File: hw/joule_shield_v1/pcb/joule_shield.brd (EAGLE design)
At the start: 160 x 100 mm, 55 parts, among them U1 BQ25892PWQFN-24, U2 FAN8623WLCSP16, U3 TPS63201PVSON-14, U4 TLV62084PWSON-8

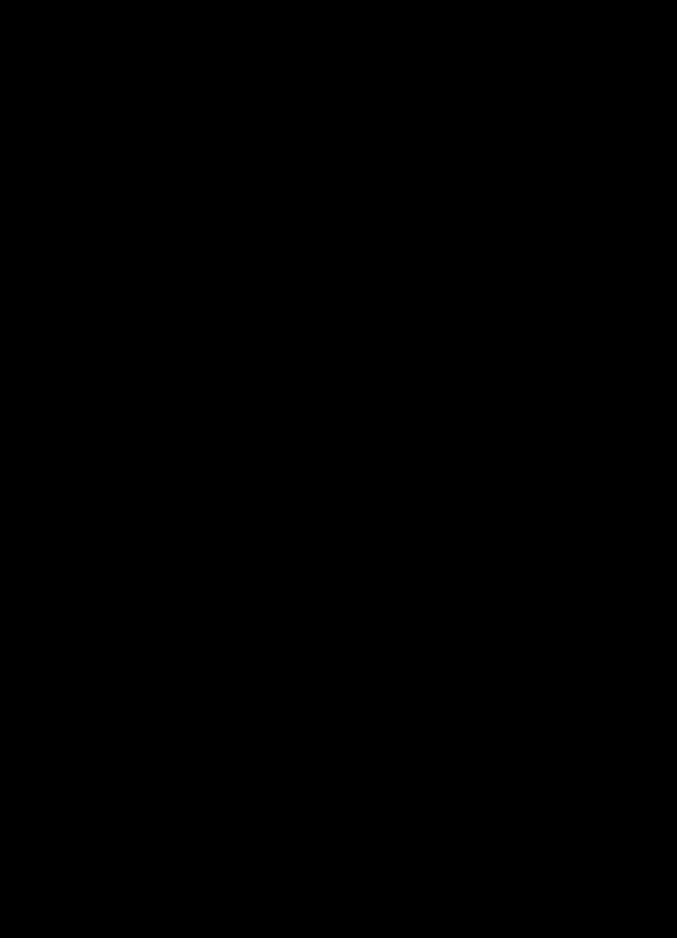
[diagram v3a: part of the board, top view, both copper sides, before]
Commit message: Schematic for USB power switch.
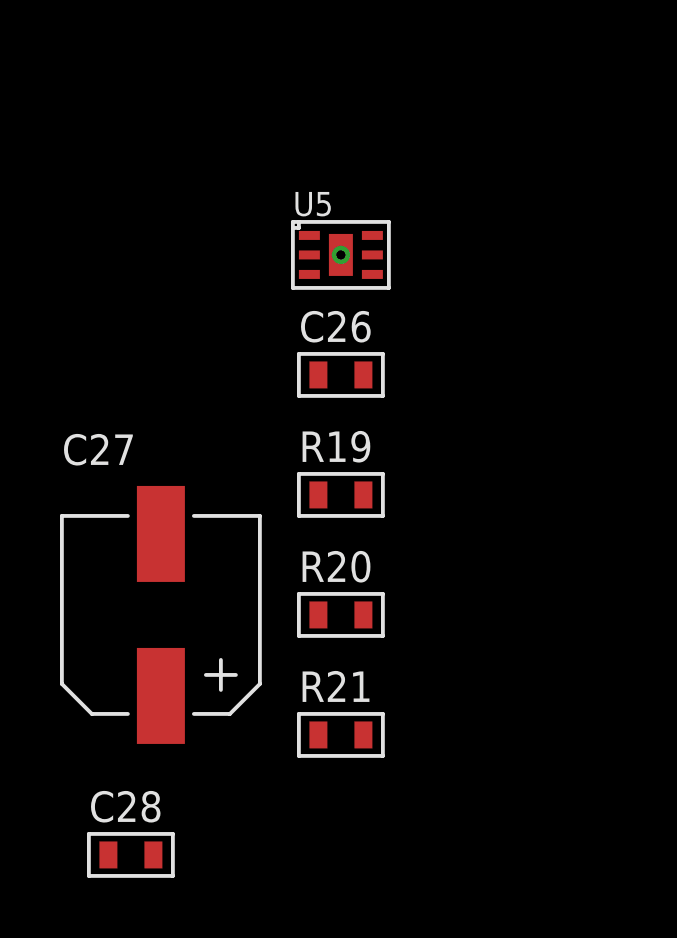
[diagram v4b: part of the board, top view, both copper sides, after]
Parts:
- added C26: 10uF, mf_passives:C0603
- added C27: 100uF, mf_passives:CP6.3MM
- added C28: 0.1uF, mf_passives:C0603
- added R19, R20: 100k, mf_passives:R0603
- added R21: 15k, mf_passives:R0603
- added U5: TPS2553PWSON-6, joule_shield:PWSON-6
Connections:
- new net N$22: R19.P$2, U5.3
- new net N$24: R20.P$2, U5.4
- new net N$29: R21.P$1, U5.2
- new net V5P0V_USBA: C27.P$1, C28.P$1, U5.1
- net GND: now also C26.P$2, C27.P$2, C28.P$2, R21.P$2, U5.5, U5.G0, U5.G1
- net V5P0V: now also C26.P$1, R19.P$1, R20.P$1, U5.6
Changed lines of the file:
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@@
 <attribute name="WATTAGE" value="" x="-109" y="67" size="1.778" layer="27" display="off"/>
+</element>
+<element name="U5" library="joule_shield" package="PWSON-6" value="TPS2553PWSON-6" x="-109" y="-3"/>
+<element name="C26" library="mf_passives" package="C0603" value="10uF" x="-109" y="-7">
+<attribute name="HOUSEPART" value="" x="-109" y="-7" size="1.778" layer="27" display="off"/>
+<attribute name="TOLERANCE" value="" x="-109" y="-7" size="1.778" layer="27" display="off"/>
+<attribute name="MPN" value="C1608X5R1E106M080AC" x="-109" y="-7" size="1.778" layer="27" display="off"/>
+<attribute name="POPULATE" value="1" x="-109" y="-7" size="1.778" layer="27" display="off"/>
+<attribute name="DIELECTRIC" value="" x="-109" y="-7" size="1.778" layer="27" display="off"/>
+<attribute name="VOLTAGE" value="" x="-109" y="-7" size="1.778" layer="27" display="off"/>
+<attribute name="URL" value="" x="-109" y="-7" size="1.778" layer="27" display="off"/>
+<attribute name="DPN" value="445-9015-1-ND" x="-109" y="-7" size="1.778" layer="27" display="off"/>
+</element>
+<element name="R19" library="mf_passives" package="R0603" value="100k" x="-109" y="-11">
+<attribute name="HOUSEPART" value="" x="-109" y="-11" size="1.778" layer="27" display="off"/>
+<attribute name="TOLERANCE" value="" x="-109" y="-11" size="1.778" layer="27" display="off"/>
+<attribute name="MPN" value="MF-RES-0603-100K" x="-109" y="-11" size="1.778" layer="27" display="off"/>
+<attribute name="POPULATE" value="1" x="-109" y="-11" size="1.778" layer="27" display="off"/>
+<attribute name="VOLTAGE" value="" x="-109" y="-11" size="1.778" layer="27" display="off"/>
+<attribute name="URL" value="" x="-109" y="-11" size="1.778" layer="27" display="off"/>
+<attribute name="WATTAGE" value="" x="-109" y="-11" size="1.778" layer="27" display="off"/>
+</element>
+<element name="R20" library="mf_passives" package="R0603" value="100k" x="-109" y="-15">
+<attribute name="HOUSEPART" value="" x="-109" y="-15" size="1.778" layer="27" display="off"/>
+<attribute name="TOLERANCE" value="" x="-109" y="-15" size="1.778" layer="27" display="off"/>
+<attribute name="MPN" value="MF-RES-0603-100K" x="-109" y="-15" size="1.778" layer="27" display="off"/>
+<attribute name="POPULATE" value="1" x="-109" y="-15" size="1.778" layer="27" display="off"/>
+<attribute name="VOLTAGE" value="" x="-109" y="-15" size="1.778" layer="27" display="off"/>
+<attribute name="URL" value="" x="-109" y="-15" size="1.778" layer="27" display="off"/>
+<attribute name="WATTAGE" value="" x="-109" y="-15" size="1.778" layer="27" display="off"/>
+</element>
+<element name="R21" library="mf_passives" package="R0603" value="15k" x="-109" y="-19">
+<attribute name="HOUSEPART" value="" x="-109" y="-19" size="1.778" layer="27" display="off"/>
+<attribute name="TOLERANCE" value="" x="-109" y="-19" size="1.778" layer="27" display="off"/>
+<attribute name="MPN" value="MF-RES-0603-15K" x="-109" y="-19" size="1.778" layer="27" display="off"/>
+<attribute name="POPULATE" value="1" x="-109" y="-19" size="1.778" layer="27" display="off"/>
+<attribute name="VOLTAGE" value="" x="-109" y="-19" size="1.778" layer="27" display="off"/>
+<attribute name="URL" value="" x="-109" y="-19" size="1.778" layer="27" display="off"/>
+<attribute name="WATTAGE" value="" x="-109" y="-19" size="1.778" layer="27" display="off"/>
+</element>
+<element name="C27" library="mf_passives" package="CP6.3MM" value="100uF" x="-115" y="-15">
+<attribute name="HOUSEPART" value="" x="-115" y="-15" size="1.778" layer="27" display="off"/>
+<attribute name="TOLERANCE" value="" x="-115" y="-15" size="1.778" layer="27" display="off"/>
+<attribute name="MPN" value="MF-CAP-6.3MM-100uF" x="-115" y="-15" size="1.778" layer="27" display="off"/>
+<attribute name="POPULATE" value="1" x="-115" y="-15" size="1.778" layer="27" display="off"/>
+<attribute name="VOTLAGE" value="" x="-115" y="-15" size="1.778" layer="27" display="off"/>
+<attribute name="URL" value="" x="-115" y="-15" size="1.778" layer="27" display="off"/>
+</element>
+<element name="C28" library="mf_passives" package="C0603" value="0.1uF" x="-116" y="-23">
+<attribute name="HOUSEPART" value="" x="-116" y="-23" size="1.778" layer="27" display="off"/>
+<attribute name="TOLERANCE" value="" x="-116" y="-23" size="1.778" layer="27" display="off"/>
+<attribute name="MPN" value="MF-CAP-0603-0.1uF" x="-116" y="-23" size="1.778" layer="27" display="off"/>
+<attribute name="POPULATE" value="1" x="-116" y="-23" size="1.778" layer="27" display="off"/>
+<attribute name="DIELECTRIC" value="" x="-116" y="-23" size="1.778" layer="27" display="off"/>
+<attribute name="VOLTAGE" value="" x="-116" y="-23" size="1.778" layer="27" display="off"/>
+<attribute name="URL" value="" x="-116" y="-23" size="1.778" layer="27" display="off"/>
 </element>
 </elements>
@@
 <contactref element="C25" pad="P$2"/>
 <contactref element="R17" pad="P$2"/>
-<wire x1="-108.25" y1="87" x2="-108.25" y2="71" width="0" layer="19" extent="1-1"/>
-<wire x1="-108.25" y1="91" x2="-108.25" y2="87" width="0" layer="19" extent="1-1"/>
-<wire x1="-108.25" y1="95" x2="-108.25" y2="91" width="0" layer="19" extent="1-1"/>
-<wire x1="-108.25" y1="105" x2="-108.25" y2="95" width="0" layer="19" extent="1-1"/>
-<wire x1="-108.25" y1="109" x2="-108.25" y2="105" width="0" layer="19" extent="1-1"/>
-<wire x1="-109" y1="113" x2="-108.25" y2="109" width="0" layer="19" extent="1-1"/>
-<wire x1="-109.95" y1="113.25" x2="-109" y2="113" width="0" layer="19" extent="1-1"/>
-<wire x1="-109.95" y1="112.75" x2="-109.95" y2="113.25" width="0" layer="19" extent="1-1"/>
-<wire x1="-77.25" y1="62" x2="-109.95" y2="113.25" width="0" layer="19" extent="1-1"/>
+<contactref element="C26" pad="P$2"/>
+<contactref element="U5" pad="G0"/>
+<contactref element="U5" pad="5"/>
+<contactref element="U5" pad="G1"/>
+<contactref element="R21" pad="P$2"/>
+<contactref element="C27" pad="P$2"/>
+<contactref element="C28" pad="P$2"/>
+<wire x1="-108.25" y1="-19" x2="-115.25" y2="-23" width="0" layer="19" extent="1-1"/>
+<wire x1="-115" y1="-12.3" x2="-108.25" y2="-19" width="0" layer="19" extent="1-1"/>
+<wire x1="-108.25" y1="-7" x2="-115" y2="-12.3" width="0" layer="19" extent="1-1"/>
+<wire x1="-107.95" y1="-3" x2="-108.25" y2="-7" width="0" layer="19" extent="1-1"/>
+<wire x1="-109" y1="-3" x2="-107.95" y2="-3" width="0" layer="19" extent="1-1"/>
+<wire x1="-77.25" y1="62" x2="-107.95" y2="-3" width="0" layer="19" extent="1-1"/>
 <wire x1="-77.25" y1="66" x2="-77.25" y2="62" width="0" layer="19" extent="1-1"/>
 <wire x1="-77.25" y1="70" x2="-77.25" y2="66" width="0" layer="19" extent="1-1"/>
@@
 <wire x1="-14.49" y1="82.55" x2="-18.3" y2="82.55" width="0" layer="19" extent="1-1"/>
 <wire x1="-22.11" y1="86.36" x2="-18.3" y2="82.55" width="0" layer="19" extent="1-1"/>
+<wire x1="-108.25" y1="109" x2="-79.4" y2="110" width="0" layer="19" extent="1-1"/>
+<wire x1="-108.25" y1="105" x2="-108.25" y2="109" width="0" layer="19" extent="1-1"/>
+<wire x1="-109" y1="113" x2="-108.25" y2="109" width="0" layer="19" extent="1-1"/>
+<wire x1="-109.95" y1="113.25" x2="-109" y2="113" width="0" layer="19" extent="1-1"/>
+<wire x1="-109.95" y1="112.75" x2="-109.95" y2="113.25" width="0" layer="19" extent="1-1"/>
+<wire x1="-108.25" y1="95" x2="-108.25" y2="105" width="0" layer="19" extent="1-1"/>
+<wire x1="-108.25" y1="91" x2="-108.25" y2="95" width="0" layer="19" extent="1-1"/>
+<wire x1="-108.25" y1="87" x2="-108.25" y2="91" width="0" layer="19" extent="1-1"/>
+<wire x1="-108.25" y1="71" x2="-108.25" y2="87" width="0" layer="19" extent="1-1"/>
 </signal>
 <signal name="N$2">
@@
 <contactref element="C12" pad="P$1"/>
 <contactref element="R12" pad="P$1"/>
+<contactref element="C26" pad="P$1"/>
+<contactref element="U5" pad="6"/>
+<contactref element="R19" pad="P$1"/>
+<contactref element="R20" pad="P$1"/>
+<wire x1="-109.75" y1="-11" x2="-109.75" y2="-15" width="0" layer="19" extent="1-1"/>
+<wire x1="-109.75" y1="-7" x2="-109.75" y2="-11" width="0" layer="19" extent="1-1"/>
+<wire x1="-107.95" y1="-2.35" x2="-109.75" y2="-7" width="0" layer="19" extent="1-1"/>
+<wire x1="-54.75" y1="67" x2="-107.95" y2="-2.35" width="0" layer="19" extent="1-1"/>
+<wire x1="-54.75" y1="71" x2="-54.75" y2="67" width="0" layer="19" extent="1-1"/>
+<wire x1="-54.75" y1="75" x2="-54.75" y2="71" width="0" layer="19" extent="1-1"/>
+<wire x1="-53.4" y1="107.2" x2="-54.75" y2="75" width="0" layer="19" extent="1-1"/>
 <wire x1="-53.8" y1="107.2" x2="-53.4" y2="107.2" width="0" layer="19" extent="1-1"/>
-<wire x1="-54.75" y1="75" x2="-53.4" y2="107.2" width="0" layer="19" extent="1-1"/>
-<wire x1="-54.75" y1="71" x2="-54.75" y2="75" width="0" layer="19" extent="1-1"/>
-<wire x1="-54.75" y1="67" x2="-54.75" y2="71" width="0" layer="19" extent="1-1"/>
 </signal>
 <signal name="VREGN">
@@
 <wire x1="-18.485" y1="71.1" x2="-19.8" y2="74.93" width="0" layer="19" extent="1-1"/>
 </signal>
+<signal name="N$22">
+<contactref element="R19" pad="P$2"/>
+<contactref element="U5" pad="3"/>
+<wire x1="-110.05" y1="-3.65" x2="-108.25" y2="-11" width="0" layer="19" extent="1-1"/>
+</signal>
+<signal name="N$24">
+<contactref element="R20" pad="P$2"/>
+<contactref element="U5" pad="4"/>
+<wire x1="-107.95" y1="-3.65" x2="-108.25" y2="-15" width="0" layer="19" extent="1-1"/>
+</signal>
+<signal name="N$29">
+<contactref element="U5" pad="2"/>
+<contactref element="R21" pad="P$1"/>
+<wire x1="-110.05" y1="-3" x2="-109.75" y2="-19" width="0" layer="19" extent="1-1"/>
+</signal>
+<signal name="V5P0V_USBA">
+<contactref element="U5" pad="1"/>
+<contactref element="C27" pad="P$1"/>
+<contactref element="C28" pad="P$1"/>
+<wire x1="-115" y1="-17.7" x2="-116.75" y2="-23" width="0" layer="19" extent="1-1"/>
+<wire x1="-110.05" y1="-2.35" x2="-115" y2="-17.7" width="0" layer="19" extent="1-1"/>
+</signal>
 </signals>

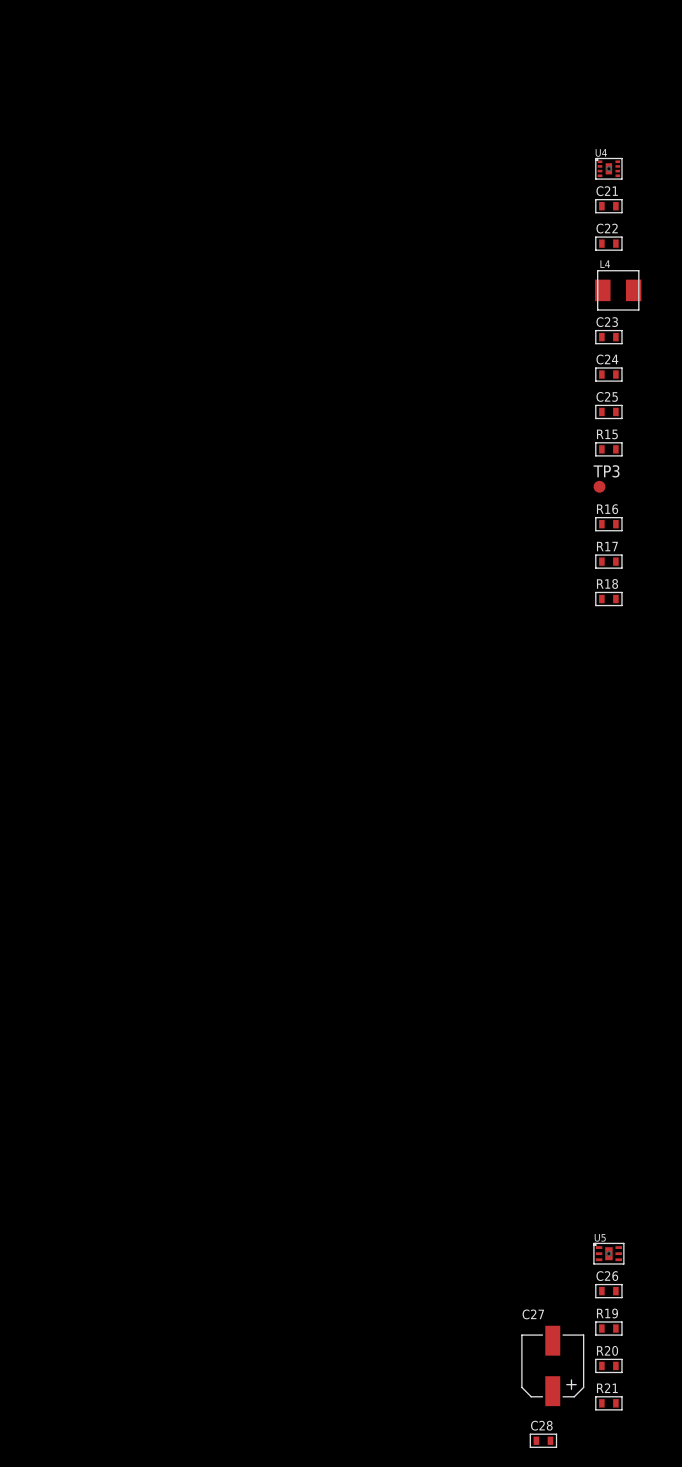
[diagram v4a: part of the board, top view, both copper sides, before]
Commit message: Schematic for serial level converters.
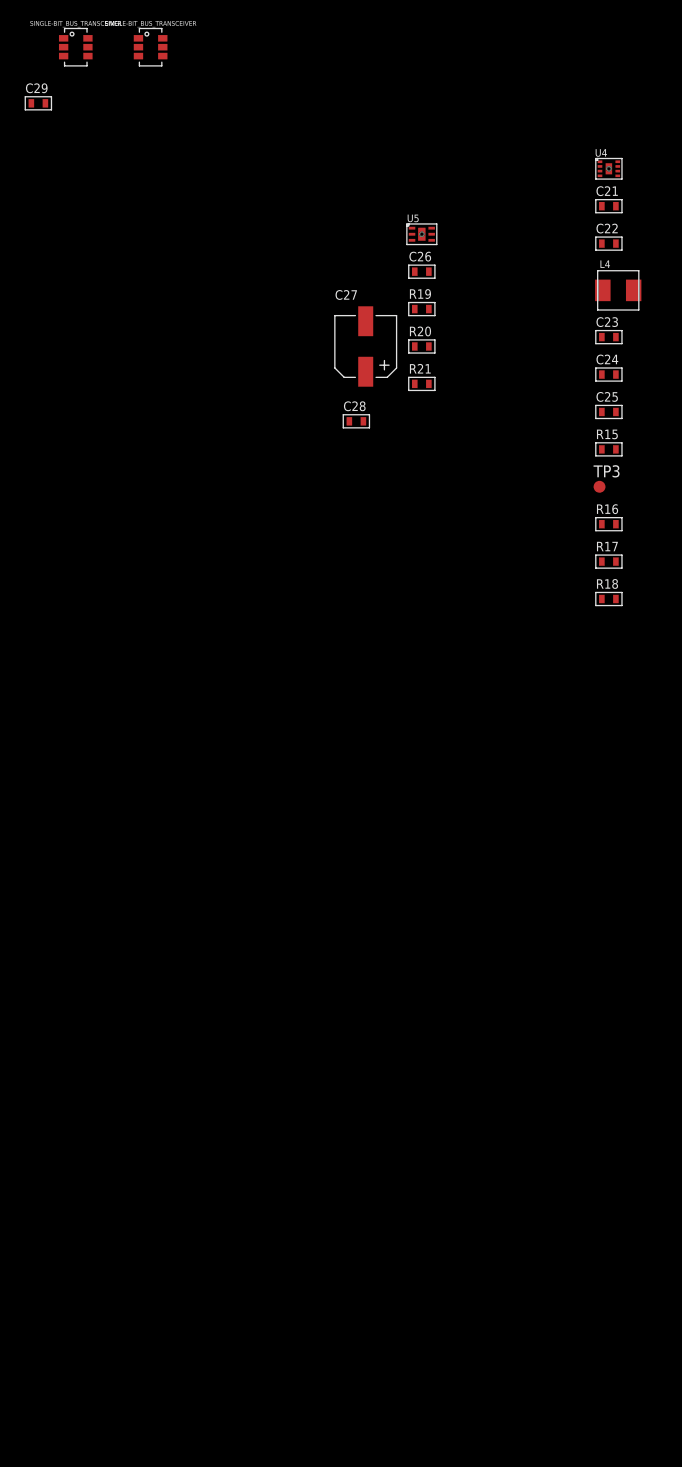
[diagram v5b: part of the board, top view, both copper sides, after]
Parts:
- added C29: 0.1uF, mf_passives:C0603
- added U6, U7: SINGLE-BIT_BUS_TRANSCEIVER, joule_shield:SOT23-6
- moved C26 110.8 mm to (-129.0, 102.0)
- moved C27 110.8 mm to (-135.0, 94.0)
- moved C28 110.8 mm to (-136.0, 86.0)
- moved R19 110.8 mm to (-129.0, 98.0)
- moved R20 110.8 mm to (-129.0, 94.0)
- moved R21 110.8 mm to (-129.0, 90.0)
- moved U5 110.8 mm to (-129.0, 106.0)
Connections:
- new net JOULE_RX_18V: U6.4
- new net JOULE_TX_18V: U7.4
- new net SERVO_RX_5V: U7.3
- new net SERVO_TX_5V: U6.3
- net GND: now also C29.P$2, U6.2, U7.2
- net V1P8V: now also C29.P$1, U6.6, U7.1, U7.5
- net V5P0V: now also U6.1, U6.5, U7.6
